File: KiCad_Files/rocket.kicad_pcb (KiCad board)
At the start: 2 copper layers, 49.7 x 90 mm, 8 parts, among them SW1 SW_DIP_x01

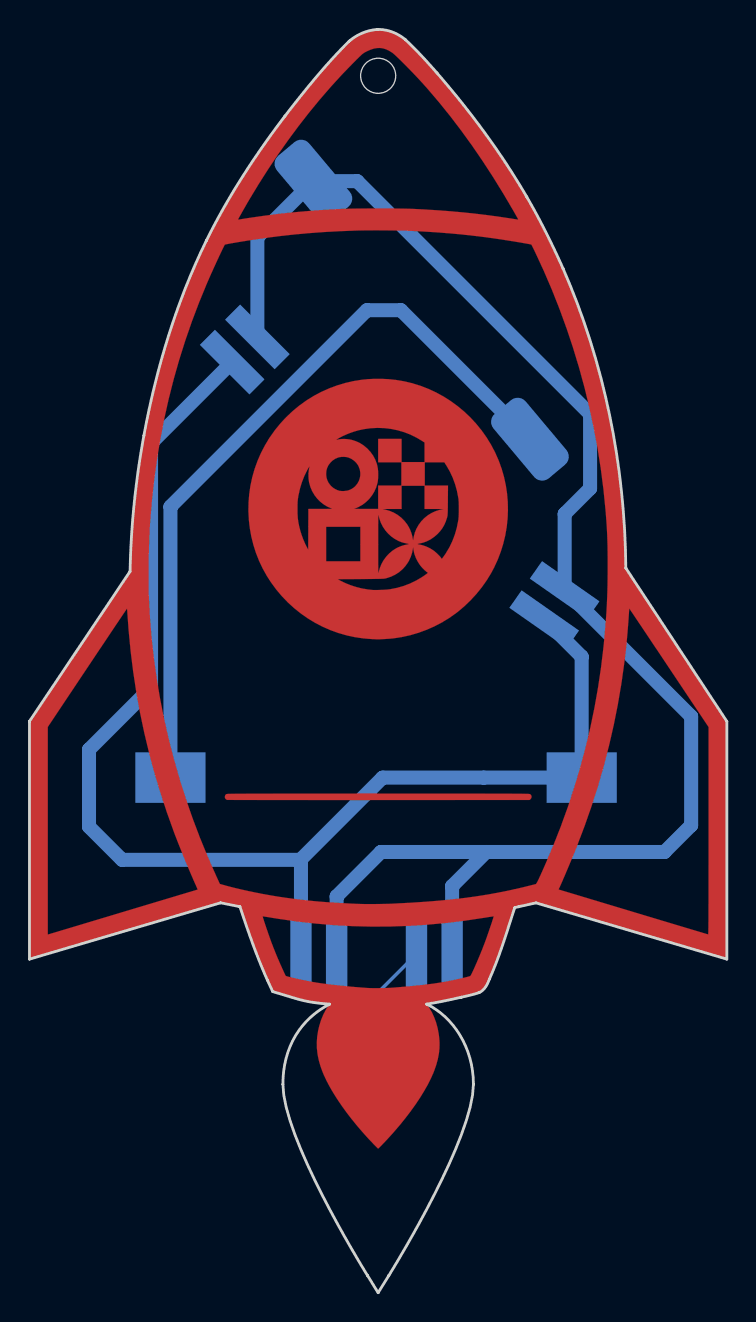
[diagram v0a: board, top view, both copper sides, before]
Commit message: fixed sharp edge on the bottom
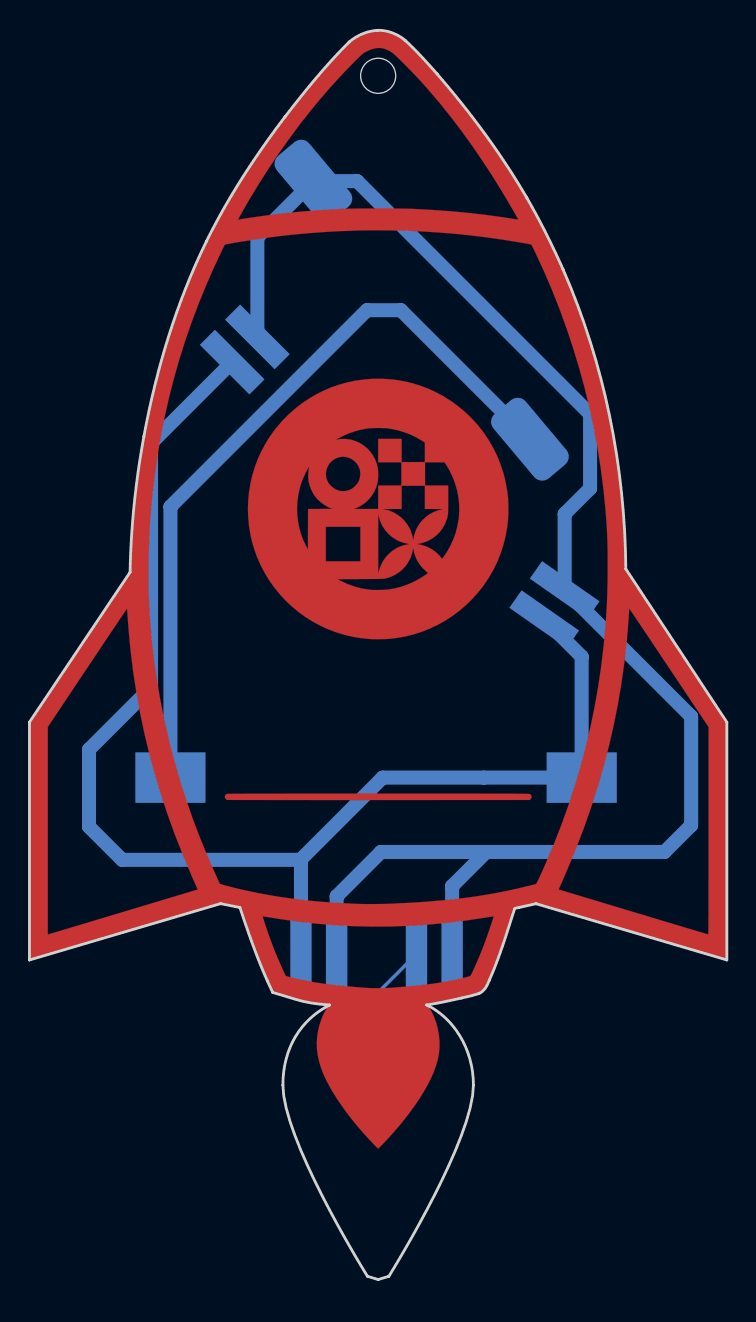
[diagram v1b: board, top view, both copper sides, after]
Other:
- board size 49.7 x 90 mm -> 49.7 x 89 mm

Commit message: moved some text
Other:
- board text added: "v2.1"
- board text removed: "v2.0"
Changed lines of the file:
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@@
     (effects (font (size 1 1) (thickness 0.15)) (justify mirror))
   )
-  (gr_text "MINT-Labs Regensburg e.V." (at 112.9 74.6) (layer "B.SilkS")
-    (effects (font (size 1 1) (thickness 0.15)) (justify mirror))
+  (gr_text "MINT-Labs Regensburg e.V." (at 112.9 74.8) (layer "B.SilkS")
+    (effects (font (size 0.8 0.8) (thickness 0.15)) (justify mirror))
   )
-  (gr_text "v2.0" (at 133.7 83.1 -90) (layer "B.SilkS")
+  (gr_text "v2.1" (at 133.7 83.1 -90) (layer "B.SilkS")
     (effects (font (size 0.75 0.75) (thickness 0.125)) (justify mirror))
   )

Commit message: added new version
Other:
- board text added: "v2.2"
- board text removed: "v2.1"
